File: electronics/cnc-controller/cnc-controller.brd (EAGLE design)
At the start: 101.6 x 72.4 mm, 117 parts, among them Q1 MOSFET-NCHANNELSMD, Q10 BSS84, Q11 BSS84, Q12 BSS84, Q13 BSS84, Q14 BSS84, Q15 BSS84, Q16 BSS84, Q17 BSS84, Q18 BSS84, Q19 BSS84, Q2 MOSFET-NCHANNELSMD, Q20 BSS84, Q21 BSS84, Q3 MOSFET-NCHANNELSMD, Q7 BSS84, Q8 BSS84, Q9 BSS84, U1 MCP41XXX, U16 USD-SOCKETNEW, X1 MSTBA2

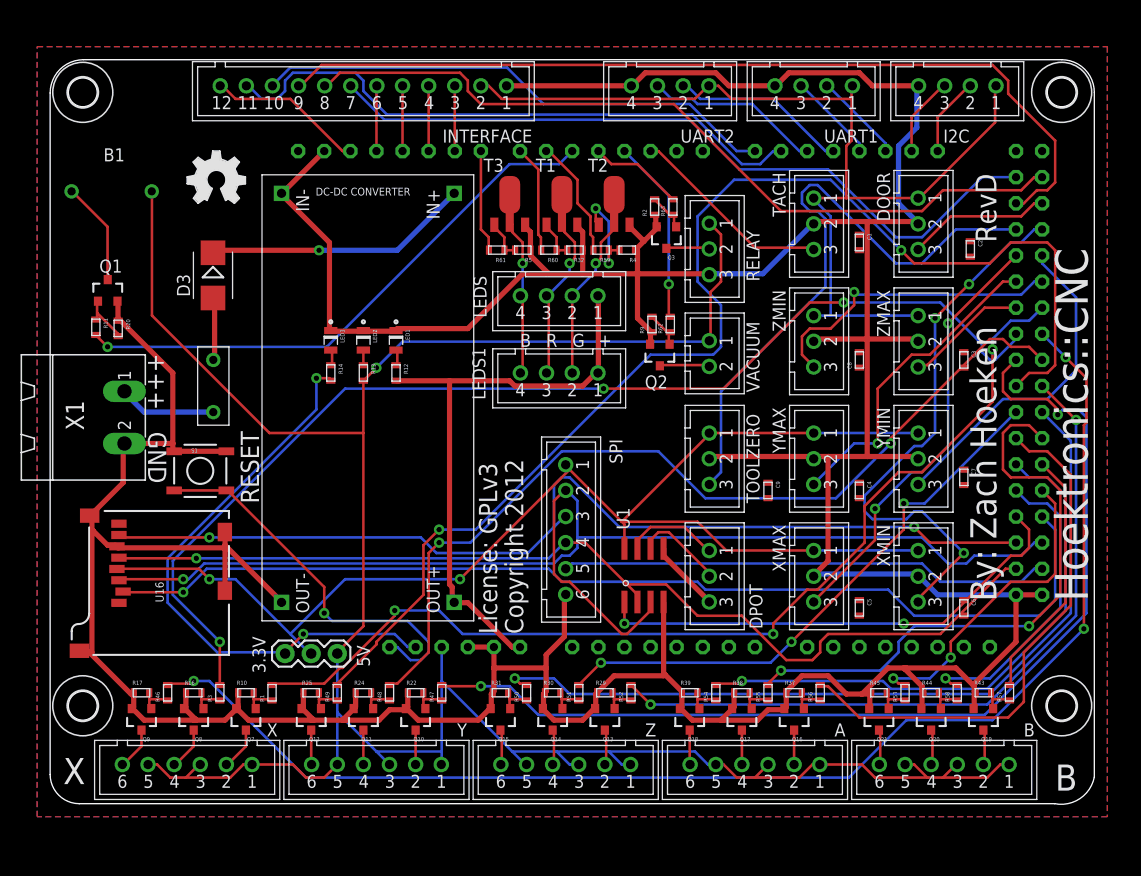
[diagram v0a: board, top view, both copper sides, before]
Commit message: updated cnc driver shield and various tweaks to milling config.
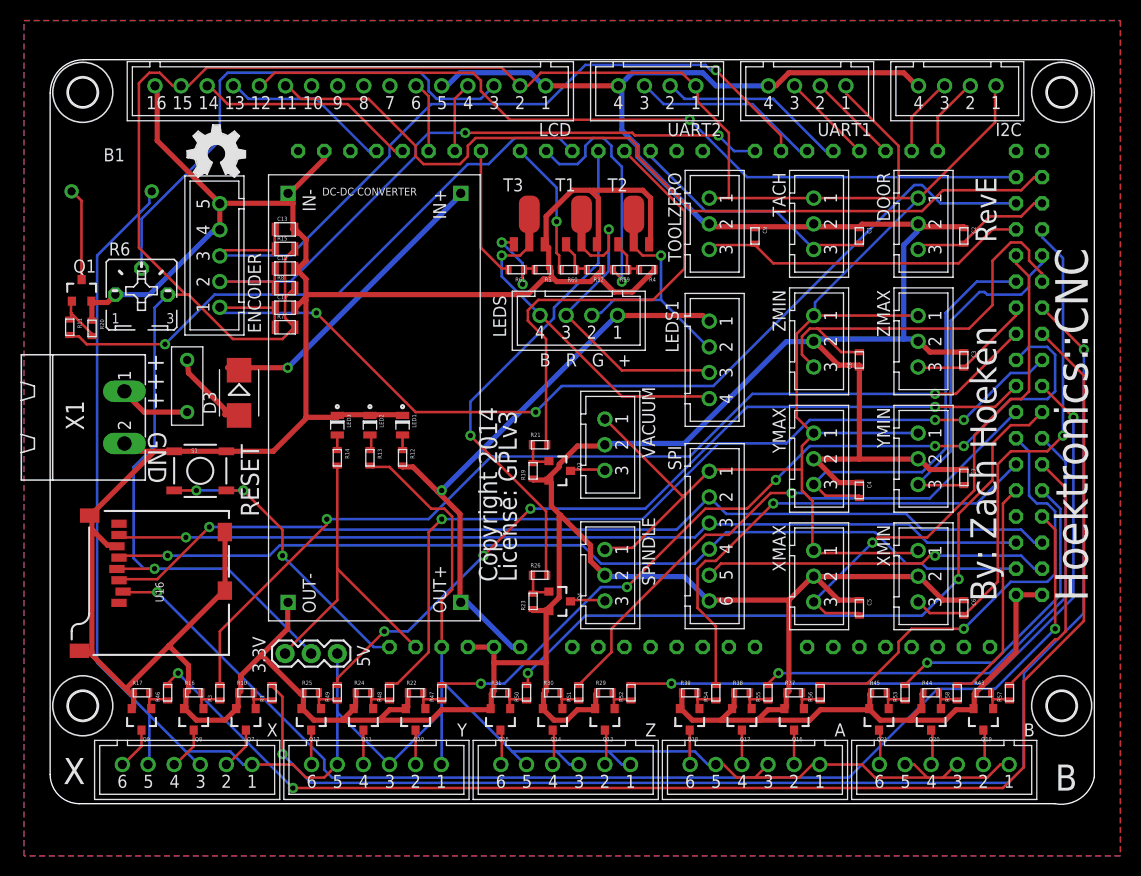
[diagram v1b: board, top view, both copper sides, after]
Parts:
- removed DPOT, RELAY: CONN-3XH-3, Hoektronics:XH-3
- removed INTERFACE: CONN-12, Hoektronics:XH-12
- removed Q2: MOSFET-NCHANNELSMD, SparkFun:SOT23-3
- removed R2, R9: 100k, Hoektronics:0603-RC
- removed R62, R63: 330, Hoektronics:0603-RC
- removed U1: MCP41XXX, Hoektronics:SO-08
- added C11, C12, C13: (no value), Hoektronics:0805-RC
- added ENCODER: CONN-5, Hoektronics:XH-5
- added LCD: CONN-16, Hoektronics:XH-16
- added Q4: BSS84, SparkFun:SOT23-3
- added R15, R7, R8: 1k, Hoektronics:0805-RC
- added R19, R23: 100k, Hoektronics:0603-RC
- added R21, R26: 330, Hoektronics:0603-RC
- added R6: (no value), pot:B25P
- added SPINDLE: CONN-3XH-3, Hoektronics:XH-3
- Q3: value MOSFET-NCHANNELSMD -> BSS84
- VACUUM: value CONN-2 -> CONN-3XH-3; device Hoektronics:XH-2 -> Hoektronics:XH-3
- moved Q3 25.0 mm to (49.5, 32.4), turned to 270 degrees
- moved C9 24.8 mm to (68.6, 55.2)
- moved TOOLZERO 22.9 mm to (64.1, 56.4)
- moved LEDS1 14.7 mm to (64.1, 43.2), turned to 270 degrees
- moved SPI 14.0 mm to (64.1, 26.0)
- moved VACUUM 12.7 mm to (54.0, 34.9)
- moved D3 11.7 mm to (18.4, 40.0)
- moved LED1 8.28 mm to (34.3, 36.8)
- moved LED2 8.28 mm to (31.1, 36.8)
- moved LED3 8.28 mm to (27.9, 36.8)
- moved R12 8.28 mm to (34.3, 33.7)
- moved R13 8.28 mm to (31.1, 33.7)
- moved R14 8.28 mm to (27.9, 33.7)
- moved LEDS 2.69 mm to (51.4, 47.5)
- moved R32 2.69 mm to (53.0, 52.0)
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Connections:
- removed net CANCEL_PIN: INTERFACE.10, U$1.D14
- removed net MENU_PIN: INTERFACE.11, U$1.D15
- removed net N$34: DPOT.1, U1.7
- removed net N$36: DPOT.3, U1.5
- removed net N$6: DPOT.2, U1.6
- removed net N$60: Q2.1, R62.1, R9.2
- removed net N$61: Q3.1, R2.2, R63.1
- removed net N$62: Q3.3, RELAY.2
- removed net N$63: Q2.3, VACUUM.2
- new net ENC_A_PIN: C12.1, ENCODER.2, R8.1, U$1.D14
- new net ENC_B_PIN: C13.1, ENCODER.3, R15.1, U$1.D15
- new net N$1: LCD.3, R6.S
- new net N$10: Q3.1, R19.2, R21.1
- new net N$11: Q4.1, R23.2, R26.1
- new net N$12: Q3.3, VACUUM.3
- new net N$13: Q4.3, SPINDLE.3
- net 5V: no longer RELAY.1, VACUUM.1
- net DEBUG_LED: no longer INTERFACE.12
- net DIGIPOT_SELECT: no longer U1.1
- net GND: now also C11.2, C12.2, C13.2, ENCODER.4, ENCODER.5, LCD.1, LCD.16, LCD.5, Q4.2, R19.1, R23.1, R6.A, SPINDLE.2, VACUUM.2; no longer INTERFACE.1, Q2.2, R2.1, R9.1, RELAY.3, U1.4
- net LCD_D4: now also LCD.11; no longer INTERFACE.8
- net LCD_D5: now also LCD.12; no longer INTERFACE.7
- net LCD_D6: now also LCD.13; no longer INTERFACE.6
- net LCD_D7: now also LCD.14; no longer INTERFACE.5
- net LCD_EN: now also LCD.6; no longer INTERFACE.4
- net LCD_RS: now also LCD.4; no longer INTERFACE.3
- net MOSI: no longer U1.3
- net OK_PIN: now also C11.1, ENCODER.1, R7.1; no longer INTERFACE.9
- net SCK: no longer U1.2
- net SPINDLE: now also R26.2; no longer R63.2
- net VACUUM: now also R21.2; no longer R62.2
- net VCC: now also LCD.15, LCD.2, R15.2, R6.E, R7.2, R8.2, SPINDLE.1, VACUUM.1; no longer INTERFACE.2, U1.8
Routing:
- net GND: track 501.9 -> 635.8 mm
- net VCC: track 236.7 -> 321.3 mm, vias 2 -> 1
- net ENC_B_PIN: track 0.00 -> 75.0 mm, vias 0 -> 1
- net ENC_A_PIN: track 0.00 -> 67.4 mm, vias 0 -> 2
- net MENU_PIN: track 59.0 -> 0.00 mm
- net CANCEL_PIN: track 51.1 -> 0.00 mm
- net N$1: track 0.00 -> 50.6 mm
- net DIGIPOT_SELECT: track 48.1 -> 0.00 mm, vias 2 -> 0
- net YENABLE: track 124.3 -> 78.5 mm, vias 2 -> 4
- net SPINDLE: track 9.19 -> 49.5 mm, vias 0 -> 1
- net XSTEP: track 98.7 -> 129.9 mm, vias 3 -> 2
- net TOOLZERO: track 60.1 -> 32.3 mm
- net 5V: track 245.2 -> 217.6 mm, vias 1 -> 0
- net VACUUM: track 18.0 -> 44.6 mm, vias 1 -> 0
- net MOSI: track 121.4 -> 95.2 mm
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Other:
- board text added: "Copyright 2014"
- board text added: "RevE"
- board text removed: "Copyright 2012"
- board text removed: "RevD"
